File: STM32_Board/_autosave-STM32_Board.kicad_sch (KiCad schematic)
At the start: 13 parts, among them SW1 SW_SPDT, U1 STM32F103C8T6

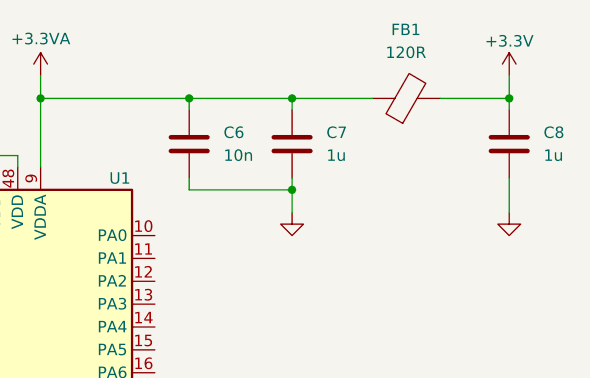
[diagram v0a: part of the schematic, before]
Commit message: Add STM32 schematic with decoupling caps, NRST, BOOT0 circuitry
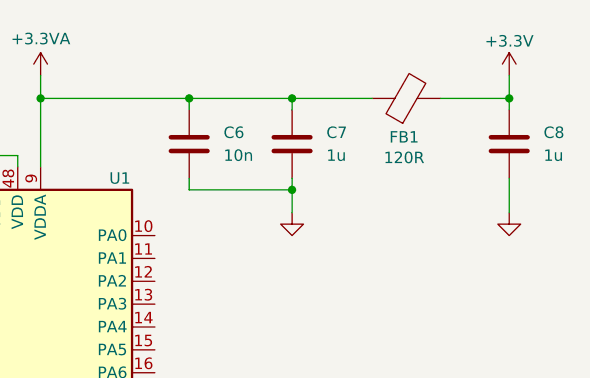
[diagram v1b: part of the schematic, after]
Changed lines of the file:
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@@
 		(on_board yes)
 		(dnp no)
-		(fields_autoplaced yes)
 		(property "Reference" "FB1"
-			(at 195.5292 40.64 90)
+			(at 195.326 52.578 90)
 			(effects
 				(font
@@
 		)
 		(property "Value" "120R"
-			(at 195.5292 43.18 90)
+			(at 195.326 54.864 90)
 			(effects
 				(font
